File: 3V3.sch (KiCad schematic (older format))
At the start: 5 parts

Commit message: annotate parts
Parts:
- gave numbers to parts that had none: 5
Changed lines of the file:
@@
 P 4350 2150
 AR Path="/5C2CE8BB" Ref="A?"  Part="1"
-AR Path="/5C2CDDAC/5C2CE8BB" Ref="A?"  Part="1"
-F 0 "A?" H 4350 2615 50  0000 C CNN
+AR Path="/5C2CDDAC/5C2CE8BB" Ref="A1"  Part="1"
+F 0 "A1" H 4350 2615 50  0000 C CNN
 F 1 "lmzm23600" H 4350 2524 50  0000 C CNN
 F 2 "LMZM23600:lmzm23600" H 4350 2150 50  0001 C CNN
@@
 P 3800 2500
 AR Path="/5C2CE8C4" Ref="#PWR?"  Part="1"
-AR Path="/5C2CDDAC/5C2CE8C4" Ref="#PWR?"  Part="1"
-F 0 "#PWR?" H 3800 2250 50  0001 C CNN
+AR Path="/5C2CDDAC/5C2CE8C4" Ref="#PWR010"  Part="1"
+F 0 "#PWR010" H 3800 2250 50  0001 C CNN
 F 1 "GND" H 3805 2327 50  0000 C CNN
 F 2 "" H 3800 2500 50  0001 C CNN
@@
 P 3550 2100
 AR Path="/5C2CE8DC" Ref="C?"  Part="1"
-AR Path="/5C2CDDAC/5C2CE8DC" Ref="C?"  Part="1"
-F 0 "C?" H 3642 2146 50  0000 L CNN
+AR Path="/5C2CDDAC/5C2CE8DC" Ref="C9"  Part="1"
+F 0 "C9" H 3642 2146 50  0000 L CNN
 F 1 "10µF" H 3642 2055 50  0000 L CNN
 F 2 "Capacitor_SMD:C_1210_3225Metric" H 3550 2100 50  0001 C CNN
@@
 P 5250 2150
 AR Path="/5C2CE8F0" Ref="C?"  Part="1"
-AR Path="/5C2CDDAC/5C2CE8F0" Ref="C?"  Part="1"
-F 0 "C?" H 5342 2196 50  0000 L CNN
+AR Path="/5C2CDDAC/5C2CE8F0" Ref="C10"  Part="1"
+F 0 "C10" H 5342 2196 50  0000 L CNN
 F 1 "33µF" H 5342 2105 50  0000 L CNN
 F 2 "Capacitor_SMD:C_1210_3225Metric" H 5250 2150 50  0001 C CNN
@@
 P 5250 2350
 AR Path="/5C2CE8F8" Ref="#PWR?"  Part="1"
-AR Path="/5C2CDDAC/5C2CE8F8" Ref="#PWR?"  Part="1"
-F 0 "#PWR?" H 5250 2100 50  0001 C CNN
+AR Path="/5C2CDDAC/5C2CE8F8" Ref="#PWR011"  Part="1"
+F 0 "#PWR011" H 5250 2100 50  0001 C CNN
 F 1 "GND" H 5255 2177 50  0000 C CNN
 F 2 "" H 5250 2350 50  0001 C CNN
@@
 P 5000 2150
 AR Path="/5C2CE900" Ref="R?"  Part="1"
-AR Path="/5C2CDDAC/5C2CE900" Ref="R?"  Part="1"
-F 0 "R?" V 5000 2150 50  0000 C CNN
+AR Path="/5C2CDDAC/5C2CE900" Ref="R12"  Part="1"
+F 0 "R12" V 5000 2150 50  0000 C CNN
 F 1 "11.5k" V 4900 2150 50  0000 C CNN
 F 2 "Resistor_SMD:R_0603_1608Metric" H 5000 2150 50  0001 C CNN
@@
 P 5000 2300
 AR Path="/5C2CE909" Ref="R?"  Part="1"
-AR Path="/5C2CDDAC/5C2CE909" Ref="R?"  Part="1"
-F 0 "R?" V 5000 2300 50  0000 C CNN
+AR Path="/5C2CDDAC/5C2CE909" Ref="R13"  Part="1"
+F 0 "R13" V 5000 2300 50  0000 C CNN
 F 1 "4.99k" V 5100 2300 50  0000 C CNN
 F 2 "Resistor_SMD:R_0603_1608Metric" H 5000 2300 50  0001 C CNN

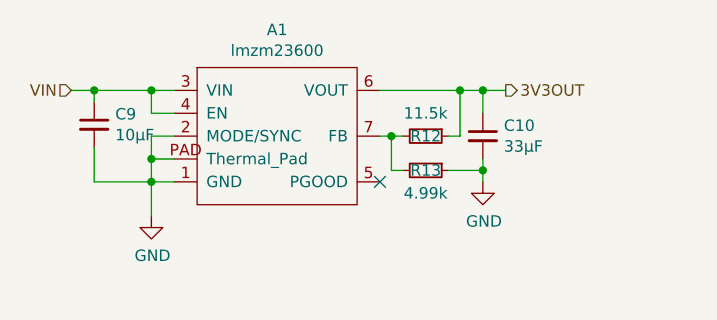
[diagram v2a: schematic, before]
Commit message: LMZM23600 from kicad libs
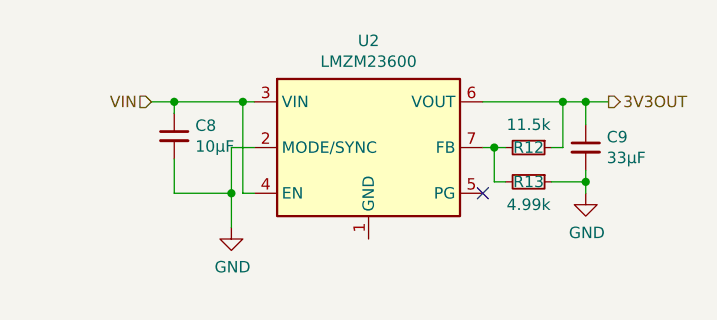
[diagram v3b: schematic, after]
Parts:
- removed A1: lmzm23600, LMZM23600:lmzm23600, symbol lmzm23600:lmzm23600
- added U2: LMZM23600, Package_LGA:Texas_SIL0010A_MicroSiP-10-1EP_3.8x3mm_P0.6mm_EP0.7x2.9mm_ThermalVias, symbol Regulator_Switching:LMZM23600
- renumbered C9 to C8, C10 to C9
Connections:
- net 3V3OUT: now also U2.6 (VOUT)
- net GND: now also U2.2 (MODE/SYNC)
- net VIN: now also U2.3 (VIN), U2.4 (EN)
- net at R12.2, R13.2: now also U2.7 (FB)
- new net: U2.1 (GND), U2.11 (GND)
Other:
- moved on the sheet: C8, C9, R12, R13
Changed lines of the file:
@@
 $EndDescr
 $Comp
-L lmzm23600:lmzm23600 A?
-U 1 1 5C2CE8BB
-P 4350 2150
-AR Path="/5C2CE8BB" Ref="A?"  Part="1"
-AR Path="/5C2CDDAC/5C2CE8BB" Ref="A1"  Part="1"
-F 0 "A1" H 4350 2615 50  0000 C CNN
-F 1 "lmzm23600" H 4350 2524 50  0000 C CNN
-F 2 "LMZM23600:lmzm23600" H 4350 2150 50  0001 C CNN
-F 3 "" H 4350 2150 50  0001 C CNN
-	1    4350 2150
+L power:GND #PWR?
+U 1 1 5C2CE8C4
+P 4150 2550
+AR Path="/5C2CE8C4" Ref="#PWR?"  Part="1"
+AR Path="/5C2CDDAC/5C2CE8C4" Ref="#PWR017"  Part="1"
+F 0 "#PWR017" H 4150 2300 50  0001 C CNN
+F 1 "GND" H 4155 2377 50  0000 C CNN
+F 2 "" H 4150 2550 50  0001 C CNN
+F 3 "" H 4150 2550 50  0001 C CNN
+	1    4150 2550
 	1    0    0    -1
 $EndComp
 Wire Wire Line
-	3800 2250 3800 2350
-Wire Wire Line
-	3800 2350 3900 2350
+	4150 2550 4150 2400
+Connection ~ 4150 2400
 $Comp
-L power:GND #PWR?
-U 1 1 5C2CE8C4
-P 3800 2500
-AR Path="/5C2CE8C4" Ref="#PWR?"  Part="1"
-AR Path="/5C2CDDAC/5C2CE8C4" Ref="#PWR010"  Part="1"
-F 0 "#PWR010" H 3800 2250 50  0001 C CNN
-F 1 "GND" H 3805 2327 50  0000 C CNN
-F 2 "" H 3800 2500 50  0001 C CNN
-F 3 "" H 3800 2500 50  0001 C CNN
-	1    3800 2500
+L Device:C_Small C?
+U 1 1 5C2CE8DC
+P 3900 2150
+AR Path="/5C2CE8DC" Ref="C?"  Part="1"
+AR Path="/5C2CDDAC/5C2CE8DC" Ref="C8"  Part="1"
+F 0 "C8" H 3992 2196 50  0000 L CNN
+F 1 "10µF" H 3992 2105 50  0000 L CNN
+F 2 "Capacitor_SMD:C_1210_3225Metric" H 3900 2150 50  0001 C CNN
+F 3 "~" H 3900 2150 50  0001 C CNN
+F 4 "50V" H 3900 2150 50  0001 C CNN "Voltage Rating"
+	1    3900 2150
 	1    0    0    -1
 $EndComp
 Wire Wire Line
-	3800 2500 3800 2350
-Connection ~ 3800 2350
-$Comp
-L Device:C_Small C?
-U 1 1 5C2CE8DC
-P 3550 2100
-AR Path="/5C2CE8DC" Ref="C?"  Part="1"
-AR Path="/5C2CDDAC/5C2CE8DC" Ref="C9"  Part="1"
-F 0 "C9" H 3642 2146 50  0000 L CNN
-F 1 "10µF" H 3642 2055 50  0000 L CNN
-F 2 "Capacitor_SMD:C_1210_3225Metric" H 3550 2100 50  0001 C CNN
-F 3 "~" H 3550 2100 50  0001 C CNN
-F 4 "50V" H 3550 2100 50  0001 C CNN "Voltage Rating"
-	1    3550 2100
-	1    0    0    -1
-$EndComp
+	3900 2250 3900 2400
 Wire Wire Line
-	3550 2200 3550 2350
+	3900 2400 4150 2400
 Wire Wire Line
-	3550 2350 3800 2350
+	4150 2200 4250 2200
 Wire Wire Line
-	3800 2150 3800 2250
-Connection ~ 3800 2250
-Wire Wire Line
-	3800 2150 3900 2150
-Wire Wire Line
-	3800 2250 3900 2250
-Wire Wire Line
-	3550 2000 3550 1950
-Wire Wire Line
-	3550 1950 3800 1950
-Connection ~ 3800 1950
-Wire Wire Line
-	3800 1950 3900 1950
-Wire Wire Line
-	3800 2050 3800 1950
-Wire Wire Line
-	3800 2050 3900 2050
+	3900 2050 3900 2000
 $Comp
 L Device:C_Small C?
 U 1 1 5C2CE8F0
-P 5250 2150
+P 5700 2200
 AR Path="/5C2CE8F0" Ref="C?"  Part="1"
-AR Path="/5C2CDDAC/5C2CE8F0" Ref="C10"  Part="1"
-F 0 "C10" H 5342 2196 50  0000 L CNN
-F 1 "33µF" H 5342 2105 50  0000 L CNN
-F 2 "Capacitor_SMD:C_1210_3225Metric" H 5250 2150 50  0001 C CNN
-F 3 "~" H 5250 2150 50  0001 C CNN
-F 4 "Low ESR" H 5250 2150 50  0001 C CNN "Notes"
-	1    5250 2150
+AR Path="/5C2CDDAC/5C2CE8F0" Ref="C9"  Part="1"
+F 0 "C9" H 5792 2246 50  0000 L CNN
+F 1 "33µF" H 5792 2155 50  0000 L CNN
+F 2 "Capacitor_SMD:C_1210_3225Metric" H 5700 2200 50  0001 C CNN
+F 3 "~" H 5700 2200 50  0001 C CNN
+F 4 "Low ESR" H 5700 2200 50  0001 C CNN "Notes"
+	1    5700 2200
 	1    0    0    -1
 $EndComp
@@
 L power:GND #PWR?
 U 1 1 5C2CE8F8
-P 5250 2350
+P 5700 2400
 AR Path="/5C2CE8F8" Ref="#PWR?"  Part="1"
-AR Path="/5C2CDDAC/5C2CE8F8" Ref="#PWR011"  Part="1"
-F 0 "#PWR011" H 5250 2100 50  0001 C CNN
-F 1 "GND" H 5255 2177 50  0000 C CNN
-F 2 "" H 5250 2350 50  0001 C CNN
-F 3 "" H 5250 2350 50  0001 C CNN
-	1    5250 2350
+AR Path="/5C2CDDAC/5C2CE8F8" Ref="#PWR018"  Part="1"
+F 0 "#PWR018" H 5700 2150 50  0001 C CNN
+F 1 "GND" H 5705 2227 50  0000 C CNN
+F 2 "" H 5700 2400 50  0001 C CNN
+F 3 "" H 5700 2400 50  0001 C CNN
+	1    5700 2400
 	1    0    0    -1
 $EndComp
 Wire Wire Line
-	5250 2050 5250 1950
+	5700 2100 5700 2000
 Wire Wire Line
-	5250 2250 5250 2300
+	5700 2300 5700 2350
 $Comp
 L Device:R_Small R?
 U 1 1 5C2CE900
-P 5000 2150
+P 5450 2200
 AR Path="/5C2CE900" Ref="R?"  Part="1"
 AR Path="/5C2CDDAC/5C2CE900" Ref="R12"  Part="1"
-F 0 "R12" V 5000 2150 50  0000 C CNN
-F 1 "11.5k" V 4900 2150 50  0000 C CNN
-F 2 "Resistor_SMD:R_0603_1608Metric" H 5000 2150 50  0001 C CNN
-F 3 "~" H 5000 2150 50  0001 C CNN
-	1    5000 2150
+F 0 "R12" V 5450 2200 50  0000 C CNN
+F 1 "11.5k" V 5350 2200 50  0000 C CNN
+F 2 "Resistor_SMD:R_0603_1608Metric" H 5450 2200 50  0001 C CNN
+F 3 "~" H 5450 2200 50  0001 C CNN
+	1    5450 2200
 	0    1    1    0
 $EndComp
 Wire Wire Line
-	4800 2150 4850 2150
+	5250 2200 5300 2200
 $Comp
 L Device:R_Small R?
 U 1 1 5C2CE909
-P 5000 2300
+P 5450 2350
 AR Path="/5C2CE909" Ref="R?"  Part="1"
 AR Path="/5C2CDDAC/5C2CE909" Ref="R13"  Part="1"
-F 0 "R13" V 5000 2300 50  0000 C CNN
-F 1 "4.99k" V 5100 2300 50  0000 C CNN
-F 2 "Resistor_SMD:R_0603_1608Metric" H 5000 2300 50  0001 C CNN
-F 3 "~" H 5000 2300 50  0001 C CNN
-	1    5000 2300
+F 0 "R13" V 5450 2350 50  0000 C CNN
+F 1 "4.99k" V 5550 2350 50  0000 C CNN
+F 2 "Resistor_SMD:R_0603_1608Metric" H 5450 2350 50  0001 C CNN
+F 3 "~" H 5450 2350 50  0001 C CNN
+	1    5450 2350
 	0    1    1    0
 $EndComp
 Wire Wire Line
-	4900 2300 4850 2300
+	5350 2350 5300 2350
 Wire Wire Line
-	4850 2300 4850 2150
-Connection ~ 4850 2150
+	5300 2350 5300 2200
+Connection ~ 5300 2200
 Wire Wire Line
-	4850 2150 4900 2150
+	5300 2200 5350 2200
 Wire Wire Line
-	5100 2300 5250 2300
-Connection ~ 5250 2300
+	5550 2350 5700 2350
+Connection ~ 5700 2350
 Wire Wire Line
-	5250 2300 5250 2350
+	5700 2350 5700 2400
 Wire Wire Line
-	5100 2150 5150 2150
+	5550 2200 5600 2200
 Wire Wire Line
-	5150 2150 5150 1950
-Connection ~ 5150 1950
+	5600 2200 5600 2000
+Connection ~ 5600 2000
 Wire Wire Line
-	5150 1950 5250 1950
-NoConn ~ 4800 2350
-Text HLabel 3450 1950 0    50   Input ~ 0
+	5600 2000 5700 2000
+NoConn ~ 5250 2400
+Text HLabel 3800 2000 0    50   Input ~ 0
 VIN
 Wire Wire Line
-	3450 1950 3550 1950
-Connection ~ 3550 1950
-Text HLabel 5350 1950 2    50   Output ~ 0
+	3800 2000 3900 2000
+Connection ~ 3900 2000
+Text HLabel 5800 2000 2    50   Output ~ 0
 3V3OUT
 Wire Wire Line
-	4800 1950 5150 1950
+	5250 2000 5600 2000
 Wire Wire Line
-	5250 1950 5350 1950
-Connection ~ 5250 1950
+	5700 2000 5800 2000
+Connection ~ 5700 2000
+$Comp
+L Regulator_Switching:LMZM23600 U2
+U 1 1 5CA5545D
+P 4750 2200
+F 0 "U2" H 4750 2667 50  0000 C CNN
+F 1 "LMZM23600" H 4750 2576 50  0000 C CNN
+F 2 "Package_LGA:Texas_SIL0010A_MicroSiP-10-1EP_3.8x3mm_P0.6mm_EP0.7x2.9mm_ThermalVias" H 4750 1350 50  0001 C CNN
+F 3 "http://www.ti.com/lit/ds/symlink/lmzm23600.pdf" H 4750 1450 50  0001 C CNN
+	1    4750 2200
+	1    0    0    -1
+$EndComp
+Wire Wire Line
+	4150 2200 4150 2400
+Wire Wire Line
+	3900 2000 4200 2000
+Wire Wire Line
+	4250 2400 4200 2400
+Wire Wire Line
+	4200 2400 4200 2000
+Connection ~ 4200 2000
+Wire Wire Line
+	4200 2000 4250 2000
 $EndSCHEMATC

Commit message: more LEDs
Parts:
- renumbered R12 to R16, R13 to R17
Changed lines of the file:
@@
 P 5450 2200
 AR Path="/5C2CE900" Ref="R?"  Part="1"
-AR Path="/5C2CDDAC/5C2CE900" Ref="R12"  Part="1"
-F 0 "R12" V 5450 2200 50  0000 C CNN
+AR Path="/5C2CDDAC/5C2CE900" Ref="R16"  Part="1"
+F 0 "R16" V 5450 2200 50  0000 C CNN
 F 1 "11.5k" V 5350 2200 50  0000 C CNN
 F 2 "Resistor_SMD:R_0603_1608Metric" H 5450 2200 50  0001 C CNN
@@
 P 5450 2350
 AR Path="/5C2CE909" Ref="R?"  Part="1"
-AR Path="/5C2CDDAC/5C2CE909" Ref="R13"  Part="1"
-F 0 "R13" V 5450 2350 50  0000 C CNN
+AR Path="/5C2CDDAC/5C2CE909" Ref="R17"  Part="1"
+F 0 "R17" V 5450 2350 50  0000 C CNN
 F 1 "4.99k" V 5550 2350 50  0000 C CNN
 F 2 "Resistor_SMD:R_0603_1608Metric" H 5450 2350 50  0001 C CNN

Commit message: layout
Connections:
- net GND: now also U2.1 (GND), U2.11 (GND)
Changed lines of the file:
@@
 P 4150 2550
 AR Path="/5C2CE8C4" Ref="#PWR?"  Part="1"
-AR Path="/5C2CDDAC/5C2CE8C4" Ref="#PWR017"  Part="1"
-F 0 "#PWR017" H 4150 2300 50  0001 C CNN
+AR Path="/5C2CDDAC/5C2CE8C4" Ref="#PWR026"  Part="1"
+F 0 "#PWR026" H 4150 2300 50  0001 C CNN
 F 1 "GND" H 4155 2377 50  0000 C CNN
 F 2 "" H 4150 2550 50  0001 C CNN
@@
 P 5700 2400
 AR Path="/5C2CE8F8" Ref="#PWR?"  Part="1"
-AR Path="/5C2CDDAC/5C2CE8F8" Ref="#PWR018"  Part="1"
-F 0 "#PWR018" H 5700 2150 50  0001 C CNN
+AR Path="/5C2CDDAC/5C2CE8F8" Ref="#PWR027"  Part="1"
+F 0 "#PWR027" H 5700 2150 50  0001 C CNN
 F 1 "GND" H 5705 2227 50  0000 C CNN
 F 2 "" H 5700 2400 50  0001 C CNN
@@
 Wire Wire Line
 	4200 2000 4250 2000
+$Comp
+L power:GND #PWR?
+U 1 1 5CA90463
+P 4750 2650
+AR Path="/5CA90463" Ref="#PWR?"  Part="1"
+AR Path="/5C2CDDAC/5CA90463" Ref="#PWR0101"  Part="1"
+F 0 "#PWR0101" H 4750 2400 50  0001 C CNN
+F 1 "GND" H 4755 2477 50  0000 C CNN
+F 2 "" H 4750 2650 50  0001 C CNN
+F 3 "" H 4750 2650 50  0001 C CNN
+	1    4750 2650
+	1    0    0    -1
+$EndComp
+Wire Wire Line
+	4750 2600 4750 2650
 $EndSCHEMATC

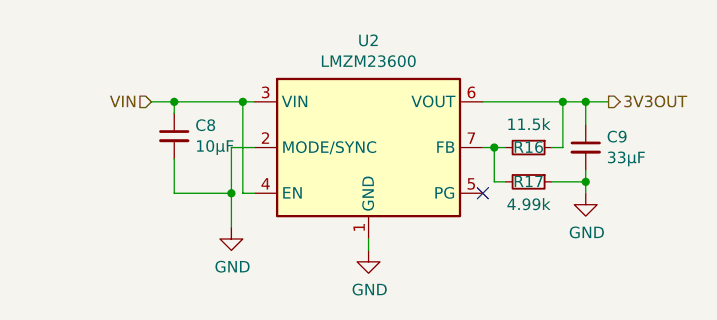
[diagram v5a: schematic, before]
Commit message: layout fixes, reannotate
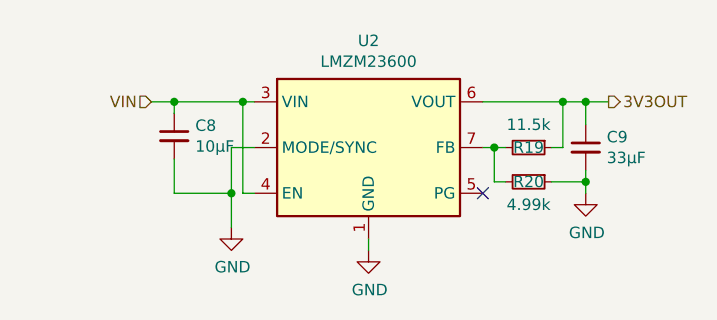
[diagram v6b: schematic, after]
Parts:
- renumbered R16 to R19, R17 to R20
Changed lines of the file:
@@
 P 4150 2550
 AR Path="/5C2CE8C4" Ref="#PWR?"  Part="1"
-AR Path="/5C2CDDAC/5C2CE8C4" Ref="#PWR026"  Part="1"
-F 0 "#PWR026" H 4150 2300 50  0001 C CNN
+AR Path="/5C2CDDAC/5C2CE8C4" Ref="#PWR035"  Part="1"
+F 0 "#PWR035" H 4150 2300 50  0001 C CNN
 F 1 "GND" H 4155 2377 50  0000 C CNN
 F 2 "" H 4150 2550 50  0001 C CNN
@@
 P 5700 2400
 AR Path="/5C2CE8F8" Ref="#PWR?"  Part="1"
-AR Path="/5C2CDDAC/5C2CE8F8" Ref="#PWR027"  Part="1"
-F 0 "#PWR027" H 5700 2150 50  0001 C CNN
+AR Path="/5C2CDDAC/5C2CE8F8" Ref="#PWR037"  Part="1"
+F 0 "#PWR037" H 5700 2150 50  0001 C CNN
 F 1 "GND" H 5705 2227 50  0000 C CNN
 F 2 "" H 5700 2400 50  0001 C CNN
@@
 P 5450 2200
 AR Path="/5C2CE900" Ref="R?"  Part="1"
-AR Path="/5C2CDDAC/5C2CE900" Ref="R16"  Part="1"
-F 0 "R16" V 5450 2200 50  0000 C CNN
+AR Path="/5C2CDDAC/5C2CE900" Ref="R19"  Part="1"
+F 0 "R19" V 5450 2200 50  0000 C CNN
 F 1 "11.5k" V 5350 2200 50  0000 C CNN
 F 2 "Resistor_SMD:R_0603_1608Metric" H 5450 2200 50  0001 C CNN
@@
 P 5450 2350
 AR Path="/5C2CE909" Ref="R?"  Part="1"
-AR Path="/5C2CDDAC/5C2CE909" Ref="R17"  Part="1"
-F 0 "R17" V 5450 2350 50  0000 C CNN
+AR Path="/5C2CDDAC/5C2CE909" Ref="R20"  Part="1"
+F 0 "R20" V 5450 2350 50  0000 C CNN
 F 1 "4.99k" V 5550 2350 50  0000 C CNN
 F 2 "Resistor_SMD:R_0603_1608Metric" H 5450 2350 50  0001 C CNN
@@
 P 4750 2650
 AR Path="/5CA90463" Ref="#PWR?"  Part="1"
-AR Path="/5C2CDDAC/5CA90463" Ref="#PWR0101"  Part="1"
-F 0 "#PWR0101" H 4750 2400 50  0001 C CNN
+AR Path="/5C2CDDAC/5CA90463" Ref="#PWR036"  Part="1"
+F 0 "#PWR036" H 4750 2400 50  0001 C CNN
 F 1 "GND" H 4755 2477 50  0000 C CNN
 F 2 "" H 4750 2650 50  0001 C CNN

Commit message: fix 3.3v regulator output cap
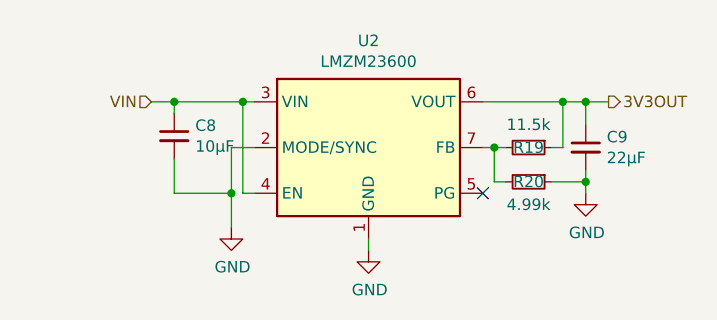
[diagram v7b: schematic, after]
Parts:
- C9: value 33µF -> 22µF; footprint Capacitor_SMD:C_1210_3225Metric -> Capacitor_SMD:C_1206_3216Metric
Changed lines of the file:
@@
 AR Path="/5C2CDDAC/5C2CE8F0" Ref="C9"  Part="1"
 F 0 "C9" H 5792 2246 50  0000 L CNN
-F 1 "33µF" H 5792 2155 50  0000 L CNN
-F 2 "Capacitor_SMD:C_1210_3225Metric" H 5700 2200 50  0001 C CNN
+F 1 "22µF" H 5792 2155 50  0000 L CNN
+F 2 "Capacitor_SMD:C_1206_3216Metric" H 5700 2200 50  0001 C CNN
 F 3 "~" H 5700 2200 50  0001 C CNN
 F 4 "Low ESR" H 5700 2200 50  0001 C CNN "Notes"
